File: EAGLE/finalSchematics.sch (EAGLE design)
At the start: 11 parts, among them IC1 STM32F103RBT, Q1 8MHz 131-220

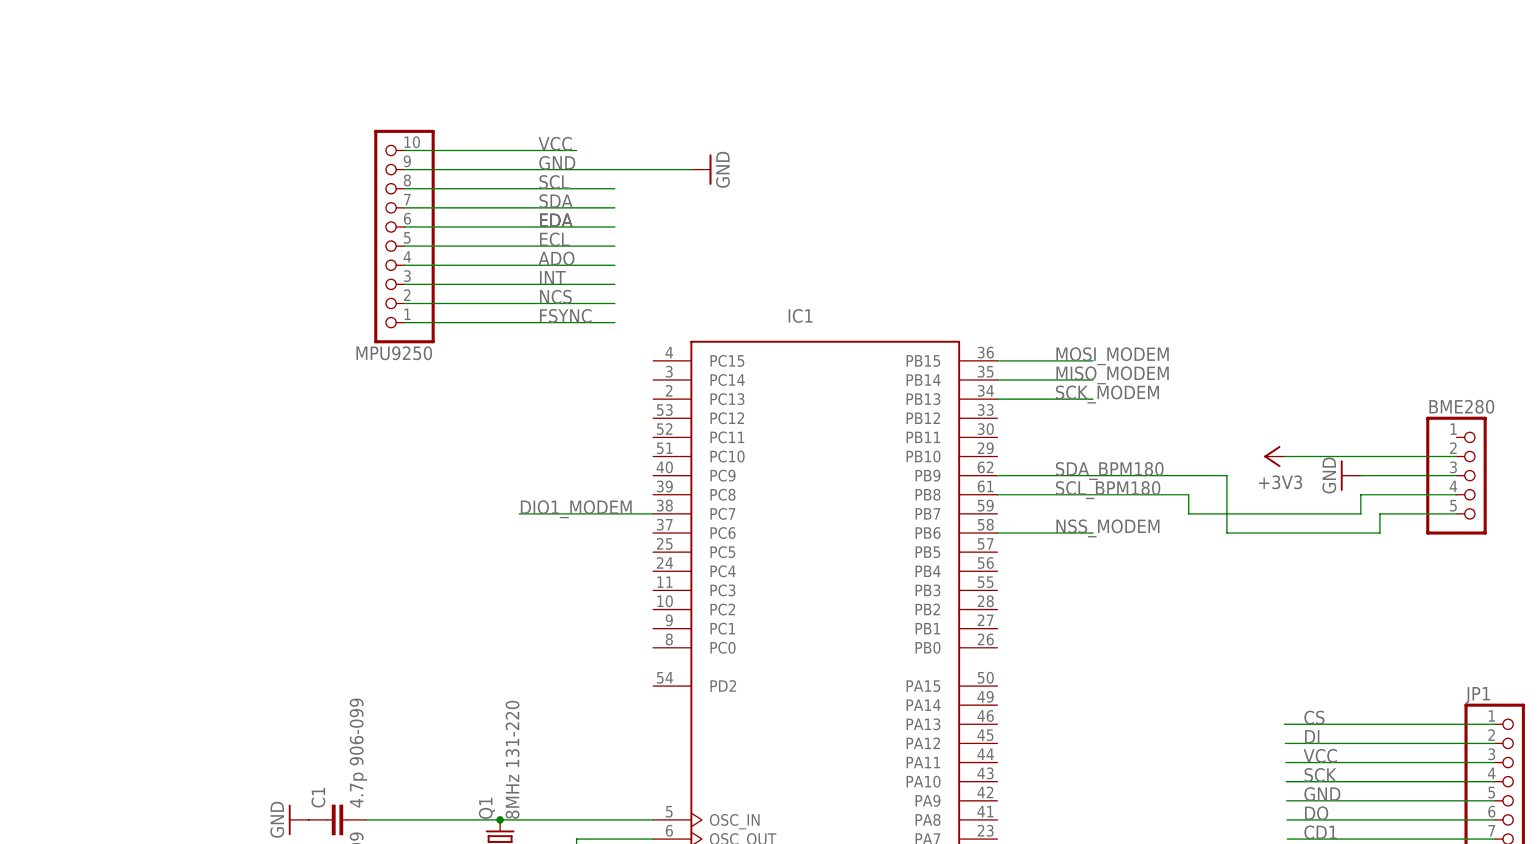
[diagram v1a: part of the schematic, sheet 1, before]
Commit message: SDfixed, Gyro fixed
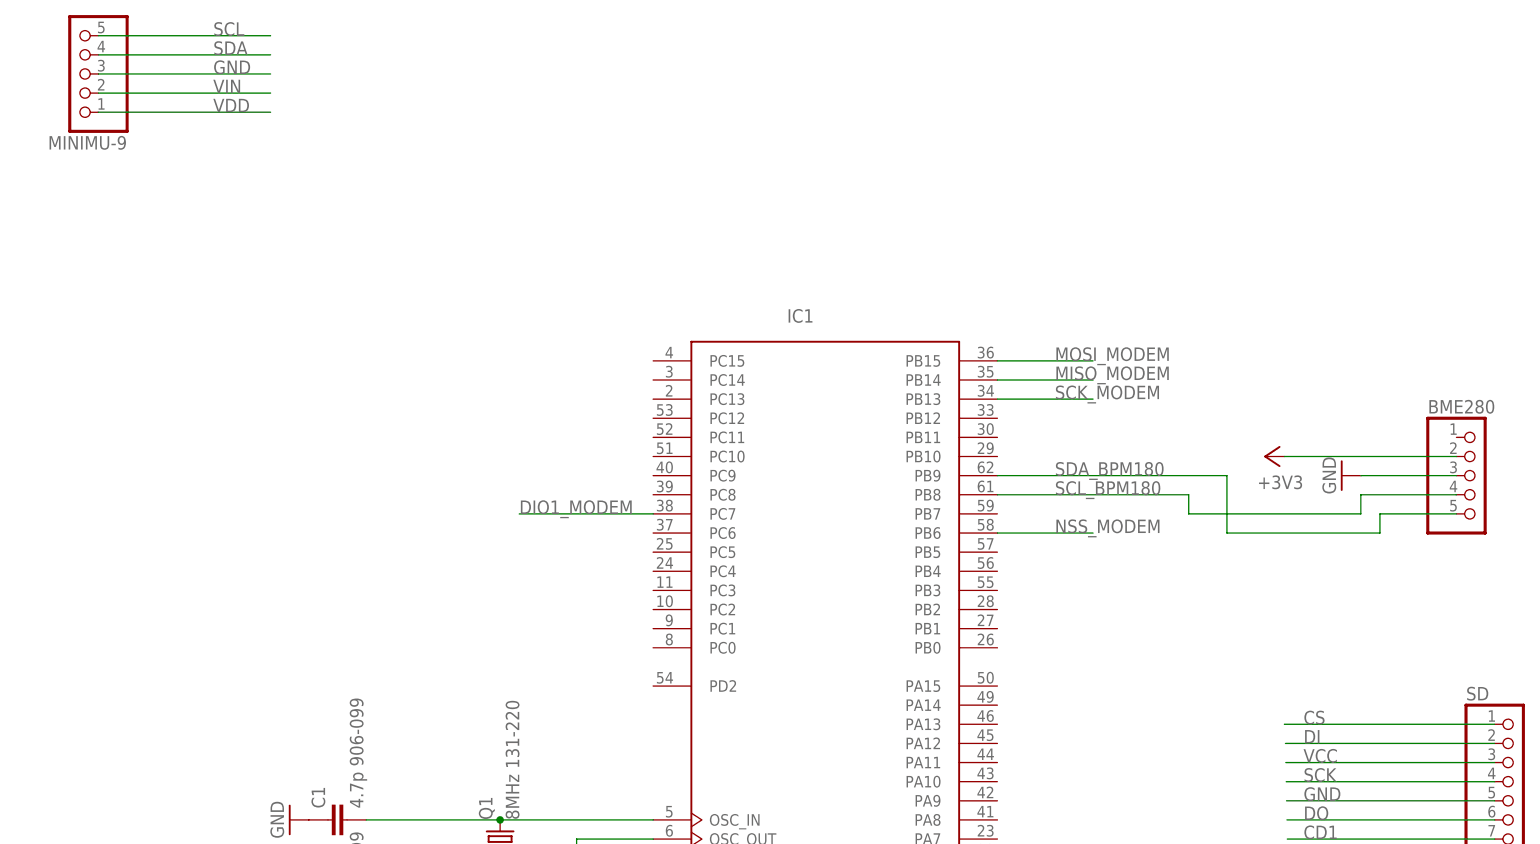
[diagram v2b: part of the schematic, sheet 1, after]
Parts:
- removed MPU9250: (no value), pinhead:PINHD-1X10
- added MINIMU-9: (no value), pinhead:PINHD-1X5
- renumbered JP1 to SD
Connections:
- removed net ADO: MPU9250.4
- removed net ECL: MPU9250.5
- removed net EDA: MPU9250.6
- removed net FSYNC: MPU9250.1
- removed net INT: MPU9250.3
- removed net NCS: MPU9250.2
- new net VDD: MINIMU-9.1
- new net VIN: MINIMU-9.2
- net GND: now also MINIMU-9.3; no longer MPU9250.9
- net SCL: now also MINIMU-9.5; no longer MPU9250.8
- net SDA: now also MINIMU-9.4; no longer MPU9250.7
- net VCC: no longer MPU9250.10
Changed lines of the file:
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@@
 <part name="+3V2" library="supply1" deviceset="+3V3" device=""/>
 <part name="GND5" library="supply1" deviceset="GND" device=""/>
-<part name="MPU9250" library="pinhead" deviceset="PINHD-1X10" device=""/>
-<part name="GND6" library="supply1" deviceset="GND" device=""/>
-<part name="JP1" library="pinhead" deviceset="PINHD-1X7" device=""/>
+<part name="SD" library="pinhead" deviceset="PINHD-1X7" device=""/>
 <part name="GPSANA" library="roundsolutions" deviceset="ANT-NSG4712-6" device=""/>
+<part name="MINIMU-9" library="pinhead" deviceset="PINHD-1X5" device=""/>
 </parts>
 <sheets>
@@
 <instance part="+3V2" gate="G$1" x="132.08" y="81.28" rot="R90"/>
 <instance part="GND5" gate="1" x="142.24" y="78.74" rot="R270"/>
-<instance part="MPU9250" gate="A" x="15.24" y="109.22" rot="R180"/>
-<instance part="GND6" gate="1" x="58.42" y="119.38" rot="R90"/>
-<instance part="JP1" gate="A" x="165.1" y="38.1"/>
+<instance part="SD" gate="A" x="165.1" y="38.1"/>
+<instance part="MINIMU-9" gate="A" x="-25.4" y="132.08" rot="R180"/>
 </instances>
 <busses>
@@
 </segment>
 <segment>
-<pinref part="MPU9250" gate="A" pin="9"/>
-<wire x1="17.78" y1="119.38" x2="55.88" y2="119.38" width="0.1524" layer="91"/>
-<label x="35.56" y="119.38" size="1.778" layer="95"/>
-<pinref part="GND6" gate="1" pin="GND"/>
-</segment>
-<segment>
-<pinref part="JP1" gate="A" pin="5"/>
+<pinref part="SD" gate="A" pin="5"/>
 <wire x1="162.56" y1="35.56" x2="134.91543125" y2="35.56" width="0.1524" layer="91"/>
 <label x="137.16" y="35.56" size="1.778" layer="95"/>
+</segment>
+<segment>
+<pinref part="MINIMU-9" gate="A" pin="3"/>
+<wire x1="-22.86" y1="132.08" x2="0" y2="132.08" width="0.1524" layer="91"/>
+<label x="-7.62" y="132.08" size="1.778" layer="95"/>
 </segment>
 </net>
@@
 <net name="VCC" class="0">
 <segment>
-<pinref part="MPU9250" gate="A" pin="10"/>
-<wire x1="17.78" y1="121.92" x2="40.64" y2="121.92" width="0.1524" layer="91"/>
-<label x="35.56" y="121.92" size="1.778" layer="95"/>
-</segment>
-<segment>
-<pinref part="JP1" gate="A" pin="3"/>
+<pinref part="SD" gate="A" pin="3"/>
 <wire x1="162.56" y1="40.64" x2="134.818734375" y2="40.64" width="0.1524" layer="91"/>
 <label x="137.16" y="40.64" size="1.778" layer="95"/>
 </segment>
 </net>
-<net name="SCL" class="0">
-<segment>
-<pinref part="MPU9250" gate="A" pin="8"/>
-<wire x1="17.78" y1="116.84" x2="45.72" y2="116.84" width="0.1524" layer="91"/>
-<label x="35.56" y="116.84" size="1.778" layer="95"/>
-</segment>
-</net>
-<net name="SDA" class="0">
-<segment>
-<pinref part="MPU9250" gate="A" pin="7"/>
-<wire x1="17.78" y1="114.3" x2="45.72" y2="114.3" width="0.1524" layer="91"/>
-<label x="35.56" y="114.3" size="1.778" layer="95"/>
-</segment>
-</net>
-<net name="EDA" class="0">
-<segment>
-<pinref part="MPU9250" gate="A" pin="6"/>
-<wire x1="17.78" y1="111.76" x2="45.72" y2="111.76" width="0.1524" layer="91"/>
-<label x="35.56" y="111.76" size="1.778" layer="95"/>
-<label x="35.56" y="111.76" size="1.778" layer="95"/>
-</segment>
-</net>
-<net name="ECL" class="0">
-<segment>
-<pinref part="MPU9250" gate="A" pin="5"/>
-<wire x1="17.78" y1="109.22" x2="45.72" y2="109.22" width="0.1524" layer="91"/>
-<label x="35.56" y="109.22" size="1.778" layer="95"/>
-</segment>
-</net>
-<net name="ADO" class="0">
-<segment>
-<pinref part="MPU9250" gate="A" pin="4"/>
-<wire x1="17.78" y1="106.68" x2="45.72" y2="106.68" width="0.1524" layer="91"/>
-<label x="35.56" y="106.68" size="1.778" layer="95"/>
-</segment>
-</net>
-<net name="INT" class="0">
-<segment>
-<pinref part="MPU9250" gate="A" pin="3"/>
-<wire x1="17.78" y1="104.14" x2="45.72" y2="104.14" width="0.1524" layer="91"/>
-<label x="35.56" y="104.14" size="1.778" layer="95"/>
-</segment>
-</net>
-<net name="NCS" class="0">
-<segment>
-<pinref part="MPU9250" gate="A" pin="2"/>
-<wire x1="17.78" y1="101.6" x2="45.72" y2="101.6" width="0.1524" layer="91"/>
-<label x="35.56" y="101.6" size="1.778" layer="95"/>
-</segment>
-</net>
-<net name="FSYNC" class="0">
-<segment>
-<pinref part="MPU9250" gate="A" pin="1"/>
-<wire x1="17.78" y1="99.06" x2="45.72" y2="99.06" width="0.1524" layer="91"/>
-<label x="35.56" y="99.06" size="1.778" layer="95"/>
-</segment>
-</net>
 <net name="CS" class="0">
 <segment>
-<pinref part="JP1" gate="A" pin="1"/>
+<pinref part="SD" gate="A" pin="1"/>
 <wire x1="162.56" y1="45.72" x2="134.62" y2="45.72" width="0.1524" layer="91"/>
 <label x="137.16" y="45.72" size="1.778" layer="95"/>
@@
 <net name="DI" class="0">
 <segment>
-<pinref part="JP1" gate="A" pin="2"/>
+<pinref part="SD" gate="A" pin="2"/>
 <wire x1="162.56" y1="43.18" x2="134.7703875" y2="43.18" width="0.1524" layer="91"/>
 <label x="137.16" y="43.18" size="1.778" layer="95"/>
@@
 <net name="SCK" class="0">
 <segment>
-<pinref part="JP1" gate="A" pin="4"/>
+<pinref part="SD" gate="A" pin="4"/>
 <wire x1="162.56" y1="38.1" x2="134.86708125" y2="38.1" width="0.1524" layer="91"/>
 <label x="137.16" y="38.1" size="1.778" layer="95"/>
@@
 <net name="DO" class="0">
 <segment>
-<pinref part="JP1" gate="A" pin="6"/>
+<pinref part="SD" gate="A" pin="6"/>
 <wire x1="162.56" y1="33.02" x2="134.963778125" y2="33.02" width="0.1524" layer="91"/>
 <label x="137.16" y="33.02" size="1.778" layer="95"/>
@@
 <net name="CD1" class="0">
 <segment>
-<pinref part="JP1" gate="A" pin="7"/>
+<pinref part="SD" gate="A" pin="7"/>
 <wire x1="162.56" y1="30.48" x2="135.012125" y2="30.48" width="0.1524" layer="91"/>
 <label x="137.16" y="30.48" size="1.778" layer="95"/>
 </segment>
 </net>
+<net name="SCL" class="0">
+<segment>
+<pinref part="MINIMU-9" gate="A" pin="5"/>
+<wire x1="-22.86" y1="137.16" x2="0" y2="137.16" width="0.1524" layer="91"/>
+<label x="-7.62" y="137.16" size="1.778" layer="95"/>
+</segment>
+</net>
+<net name="SDA" class="0">
+<segment>
+<pinref part="MINIMU-9" gate="A" pin="4"/>
+<wire x1="-22.86" y1="134.62" x2="0" y2="134.62" width="0.1524" layer="91"/>
+<label x="-7.62" y="134.62" size="1.778" layer="95"/>
+</segment>
+</net>
+<net name="VIN" class="0">
+<segment>
+<pinref part="MINIMU-9" gate="A" pin="2"/>
+<wire x1="-22.86" y1="129.54" x2="0" y2="129.54" width="0.1524" layer="91"/>
+<label x="-7.62" y="129.54" size="1.778" layer="95"/>
+</segment>
+</net>
+<net name="VDD" class="0">
+<segment>
+<pinref part="MINIMU-9" gate="A" pin="1"/>
+<wire x1="-22.86" y1="127" x2="0" y2="127" width="0.1524" layer="91"/>
+<label x="-7.62" y="127" size="1.778" layer="95"/>
+</segment>
+</net>

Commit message: Update
WIP
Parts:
- removed SD: (no value), pinhead:PINHD-1X7
- added P1: DM3CS-SF, DM3CS-SF:DM3CS-SF
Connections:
- removed net CD1: SD.7
- removed net DI: SD.2
- removed net DO: SD.6
- removed net SCL_BPM180: BME280.4, IC1MCU.PB8
- removed net SDA_BPM180: BME280.5, IC1MCU.PB9
- removed net VCC: SD.3
- removed net VDD: MINIMU-9.1
- removed net VIN: MINIMU-9.2
- new net MISO: IC1MCU.PB14, P1.DAT0
- new net MOSI: IC1MCU.PB15, P1.CMD
- net +3V3: now also MINIMU-9.5, P1.VDD
- net CS: now also IC1MCU.PA10, P1.DAT3; no longer SD.1
- net GND: now also P1.VSS; no longer SD.5
- net MISO_MODEM: no longer IC1MCU.PB14
- net MOSI_MODEM: no longer IC1MCU.PB15
- net SCK: now also IC1MCU.PB13, P1.CLK; no longer SD.4
- net SCK_MODEM: no longer IC1MCU.PB13
- net SCL: now also BME280.4, IC1MCU.PB8, MINIMU-9.1; no longer MINIMU-9.5
- net SDA: now also BME280.5, IC1MCU.PB9, MINIMU-9.2; no longer MINIMU-9.4

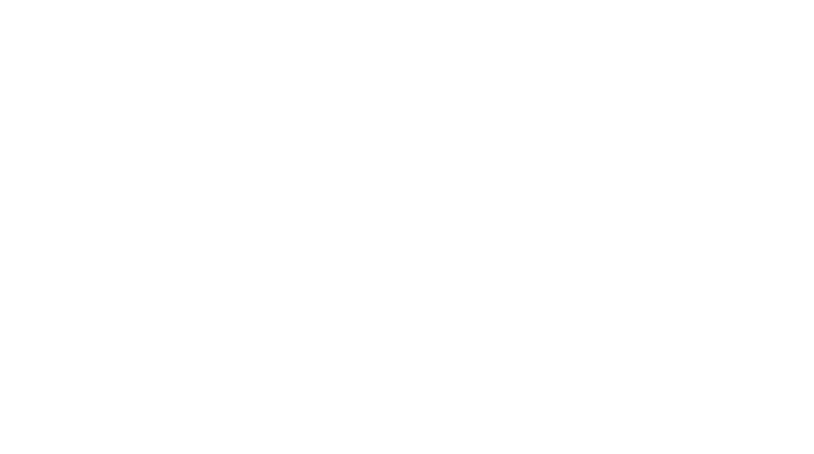
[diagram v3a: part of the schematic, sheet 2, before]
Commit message: Add GPS components
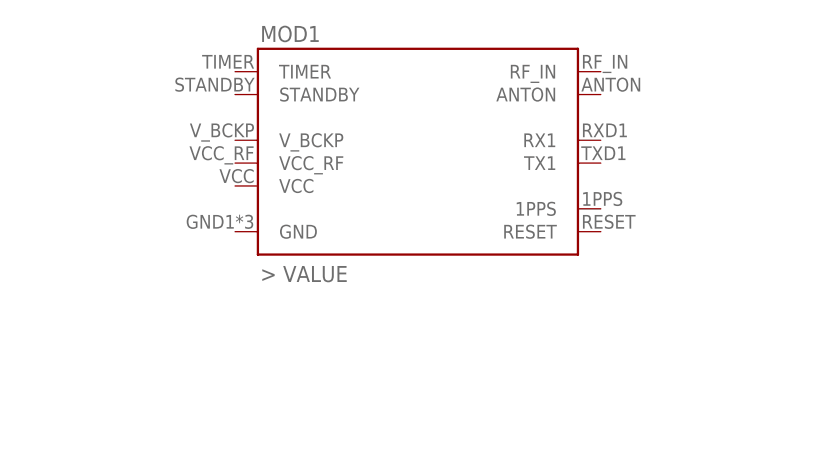
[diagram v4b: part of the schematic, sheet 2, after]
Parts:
- added MOD1: (no value), components:L70B-GPS
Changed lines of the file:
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@@
 <?xml version="1.0" encoding="utf-8"?>
 <!DOCTYPE eagle SYSTEM "eagle.dtd">
-<eagle version="8.0.0">
+<eagle version="8.0.1">
 <drawing>
 <settings>
@@
 <part name="GND7" library="supply1" deviceset="GND" device=""/>
 <part name="+3V4" library="supply1" deviceset="+3V3" device=""/>
+<part name="MOD1" library="components" deviceset="L70B-GPS" device=""/>
 </parts>
 <sheets>
@@
 <instance part="+3V1" gate="G$1" x="53.34" y="91.44" rot="R90"/>
 <instance part="GPSANA" gate="G$1" x="165.1" y="152.4"/>
+<instance part="MOD1" gate="G$1" x="96.52" y="152.4"/>
 </instances>
 <busses>

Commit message: Finish modules
All modules except SD card imported in the schematic. Board still to-do
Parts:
- removed GPSANA: ANT-NSG4712-6, roundsolutions:ANT-NSG4712-6
- added MOD2: (no value), BME280:BME280
- added MOD3: IMU04A, IMU:IMU04A
- BME280: device pinhead:PINHD-1X5/90 -> pinhead:PINHD-1X4
- MOD1: value (none) -> GPS
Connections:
- new net RX: MOD1.RX1
- new net TX: MOD1.TX1
- net +3V3: now also BME280.1; no longer BME280.2
- net GND: now also BME280.2, MOD1.GND; no longer BME280.3
- net SCL: now also BME280.3; no longer BME280.4
- net SDA: now also BME280.4; no longer BME280.5
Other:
- moved on the sheet: MOD1
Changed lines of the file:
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@@
 <?xml version="1.0" encoding="utf-8"?>
 <!DOCTYPE eagle SYSTEM "eagle.dtd">
-<eagle version="8.0.1">
+<eagle version="8.0.0">
 <drawing>
 <settings>
@@
 <layer number="48" name="Document" color="7" fill="1" visible="no" active="no"/>
 <layer number="49" name="Reference" color="7" fill="1" visible="no" active="no"/>
-<layer number="51" name="tDocu" color="6" fill="9" visible="no" active="no"/>
+<layer number="51" name="tDocu" color="7" fill="1" visible="no" active="no"/>
 <layer number="52" name="bDocu" color="7" fill="1" visible="no" active="no"/>
 <layer number="90" name="Modules" color="5" fill="1" visible="yes" active="yes"/>
@@
 <part name="RADIOANA" library="discrete" deviceset="ANTENNA" device=""/>
 <part name="+3V1" library="supply1" deviceset="+3V3" device=""/>
-<part name="BME280" library="pinhead" deviceset="PINHD-1X5" device="/90"/>
 <part name="+3V2" library="supply1" deviceset="+3V3" device=""/>
 <part name="GND5" library="supply1" deviceset="GND" device=""/>
-<part name="GPSANA" library="roundsolutions" deviceset="ANT-NSG4712-6" device=""/>
 <part name="MINIMU-9" library="pinhead" deviceset="PINHD-1X5" device=""/>
 <part name="P1" library="DM3CS-SF" deviceset="DM3CS-SF" device=""/>
@@
 <part name="GND7" library="supply1" deviceset="GND" device=""/>
 <part name="+3V4" library="supply1" deviceset="+3V3" device=""/>
-<part name="MOD1" library="components" deviceset="L70B-GPS" device=""/>
+<part name="MOD1" library="components" deviceset="L70B-GPS" device="" value="GPS"/>
+<part name="MOD2" library="BME280" deviceset="BME280" device=""/>
+<part name="BME280" library="pinhead" deviceset="PINHD-1X4" device=""/>
+<part name="MOD3" library="IMU" deviceset="IMU04A" device=""/>
+<part name="GND8" library="supply1" deviceset="GND" device=""/>
 </parts>
 <sheets>
@@
 <instance part="R1" gate="G$1" x="45.72" y="7.62"/>
 <instance part="GND3" gate="1" x="33.02" y="7.62" rot="R270"/>
-<instance part="BME280" gate="A" x="160.02" y="78.74"/>
 <instance part="+3V2" gate="G$1" x="132.08" y="81.28" rot="R90"/>
 <instance part="GND5" gate="1" x="142.24" y="78.74" rot="R270"/>
@@
 <instance part="GND7" gate="1" x="12.7" y="132.08" rot="R90"/>
 <instance part="+3V4" gate="G$1" x="2.54" y="137.16" rot="R270"/>
+<instance part="MOD2" gate="G$1" x="190.5" y="73.66"/>
+<instance part="BME280" gate="A" x="160.02" y="76.2"/>
+<instance part="MOD3" gate="G$1" x="-53.34" y="144.78" rot="R180"/>
 </instances>
 <busses>
@@
 </segment>
 <segment>
-<pinref part="BME280" gate="A" pin="3"/>
 <wire x1="157.48" y1="78.74" x2="144.78" y2="78.74" width="0.1524" layer="91"/>
 <pinref part="GND5" gate="1" pin="GND"/>
+<pinref part="BME280" gate="A" pin="2"/>
 </segment>
 <segment>
@@
 <net name="+3V3" class="0">
 <segment>
-<pinref part="BME280" gate="A" pin="2"/>
 <wire x1="157.48" y1="81.28" x2="134.62" y2="81.28" width="0.1524" layer="91"/>
 <pinref part="+3V2" gate="G$1" pin="+3V3"/>
+<pinref part="BME280" gate="A" pin="1"/>
 </segment>
 <segment>
@@
 <pinref part="IC1" gate="MCU" pin="PB8"/>
 <label x="104.14" y="76.2" size="1.778" layer="95"/>
-<pinref part="BME280" gate="A" pin="4"/>
 <wire x1="157.48" y1="76.2" x2="144.78" y2="76.2" width="0.1524" layer="91"/>
 <wire x1="144.78" y1="76.2" x2="144.78" y2="73.66" width="0.1524" layer="91"/>
@@
 <wire x1="124.46" y1="119.38" x2="124.46" y2="73.66" width="0.1524" layer="91"/>
 <junction x="124.46" y="73.66"/>
+<pinref part="BME280" gate="A" pin="3"/>
 </segment>
 </net>
@@
 <pinref part="IC1" gate="MCU" pin="PB9"/>
 <label x="104.14" y="78.74" size="1.778" layer="95"/>
-<pinref part="BME280" gate="A" pin="5"/>
 <wire x1="157.48" y1="73.66" x2="147.32" y2="73.66" width="0.1524" layer="91"/>
 <wire x1="147.32" y1="73.66" x2="147.32" y2="71.12" width="0.1524" layer="91"/>
@@
 <wire x1="121.92" y1="121.92" x2="121.92" y2="78.74" width="0.1524" layer="91"/>
 <junction x="121.92" y="78.74"/>
+<pinref part="BME280" gate="A" pin="4"/>
 </segment>
 </net>
@@
 <instance part="RADIOANA" gate="A" x="142.24" y="93.98" rot="R270"/>
 <instance part="+3V1" gate="G$1" x="53.34" y="91.44" rot="R90"/>
-<instance part="GPSANA" gate="G$1" x="165.1" y="152.4"/>
-<instance part="MOD1" gate="G$1" x="96.52" y="152.4"/>
+<instance part="MOD1" gate="G$1" x="86.36" y="152.4"/>
+<instance part="GND8" gate="1" x="58.42" y="142.24"/>
 </instances>
 <busses>
@@
 <pinref part="GND4" gate="1" pin="GND"/>
 </segment>
+<segment>
+<pinref part="MOD1" gate="G$1" pin="GND"/>
+<wire x1="66.04" y1="144.78" x2="58.42" y2="144.78" width="0.1524" layer="91"/>
+<pinref part="GND8" gate="1" pin="GND"/>
+</segment>
 </net>
 <net name="+3V3" class="0">
@@
 </segment>
 </net>
+<net name="RX" class="0">
+<segment>
+<pinref part="MOD1" gate="G$1" pin="RX1"/>
+<wire x1="106.68" y1="154.94" x2="139.7" y2="154.94" width="0.1524" layer="91"/>
+<label x="134.62" y="154.94" size="1.778" layer="95"/>
+</segment>
+</net>
+<net name="TX" class="0">
+<segment>
+<pinref part="MOD1" gate="G$1" pin="TX1"/>
+<wire x1="106.68" y1="152.4" x2="139.7" y2="152.4" width="0.1524" layer="91"/>
+<label x="134.62" y="152.4" size="1.778" layer="95"/>
+</segment>
+</net>
